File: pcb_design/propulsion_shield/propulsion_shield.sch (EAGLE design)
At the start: 62 parts

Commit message: [propulsion_shield] First draft of components placement + Bugfixes in schematics
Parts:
- JP14: value (none) -> M16PTH; device SparkFun-Connectors:M03PTH -> SparkFun-Connectors:M16PTH
- JP9: value M16PTH -> (none); device SparkFun-Connectors:M16PTH -> SparkFun-Connectors:M03PTH
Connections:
- net GND: now also JP14.1, JP9.2; no longer JP14.2, JP9.1
- net MOT1_1: now also JP5.2; no longer JP5.3
- net MOT1_2: now also JP5.3; no longer JP5.2
- net MOT2_1: now also JP6.2; no longer JP6.3
- net MOT2_2: now also JP6.3; no longer JP6.2
- net MOT3_1: now also JP7.2; no longer JP7.3
- net MOT3_2: now also JP7.3; no longer JP7.2
- net SCL_HW: no longer SJ2.2, SJ4.2
- net SDA_HW: now also SJ2.2, SJ4.2
- net SHARP_1: now also JP9.3; no longer JP10.3
- net SHARP_2: now also JP10.3; no longer JP11.3
- net SHARP_3: now also JP11.3; no longer JP12.3
- net SHARP_4: now also JP12.3; no longer JP13.3
- net SHARP_5: now also JP13.3; no longer JP14.3
- net UI_0: now also JP14.3; no longer JP9.3
- net UI_1: now also JP14.4; no longer JP9.4
- net UI_10: now also JP14.13; no longer JP9.13
- net UI_11: now also JP14.14; no longer JP9.14
- net UI_12: now also JP14.15; no longer JP9.15
- net UI_13: now also JP14.16; no longer JP9.16
- net UI_2: now also JP14.5; no longer JP9.5
- net UI_3: now also JP14.6; no longer JP9.6
- net UI_4: now also JP14.7; no longer JP9.7
- net UI_5: now also JP14.8; no longer JP9.8
- net UI_6: now also JP14.9; no longer JP9.9
- net UI_7: now also JP14.10; no longer JP9.10
- net UI_8: now also JP14.11; no longer JP9.11
- net UI_9: now also JP14.12; no longer JP9.12
- net VCC: now also JP14.2, JP9.1; no longer JP14.1, JP9.2
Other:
- moved on the sheet: JP10, JP11, JP12, JP13

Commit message: [propulsion_shield] Full routing of the PCB
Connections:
- net SCL_SW1: now also IC1.PK6(ADC14/PCINT22); no longer IC1.PK7(ADC15/PCINT23)
- net SDA_SW1: now also IC1.PK7(ADC15/PCINT23); no longer IC1.PK6(ADC14/PCINT22)
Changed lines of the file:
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@@
 <net name="SDA_SW1" class="0">
-<segment>
-<pinref part="IC1" gate="G$1" pin="PK6(ADC14/PCINT22)"/>
-<wire x1="15.24" y1="109.22" x2="2.54" y2="109.22" width="0.2032" layer="91"/>
-<label x="2.54" y="109.22" size="1.778" layer="95"/>
-</segment>
 <segment>
 <pinref part="JP22" gate="G$1" pin="1"/>
@@
 <label x="205.74" y="66.04" size="1.778" layer="95"/>
 </segment>
-</net>
-<net name="SCL_SW1" class="0">
 <segment>
 <pinref part="IC1" gate="G$1" pin="PK7(ADC15/PCINT23)"/>
@@
 <label x="2.54" y="106.68" size="1.778" layer="95"/>
 </segment>
+</net>
+<net name="SCL_SW1" class="0">
 <segment>
 <pinref part="JP22" gate="G$1" pin="2"/>
@@
 <label x="205.74" y="68.58" size="1.778" layer="95"/>
 </segment>
+<segment>
+<pinref part="IC1" gate="G$1" pin="PK6(ADC14/PCINT22)"/>
+<wire x1="15.24" y1="109.22" x2="2.54" y2="109.22" width="0.2032" layer="91"/>
+<label x="2.54" y="109.22" size="1.778" layer="95"/>
+</segment>
 </net>

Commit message: [propulsion_shield] Added Silkscreen on board
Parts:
- R13: value 470 -> 10k
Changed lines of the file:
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@@
 <part name="S2" library="SparkFun-Electromechanical" deviceset="SWITCH-MOMENTARY-2" device="PTH"/>
 <part name="GND33" library="SparkFun-Aesthetics" deviceset="GND" device=""/>
-<part name="R13" library="SparkFun-Passives" deviceset="RESISTOR" device="1206" value="470"/>
+<part name="R13" library="SparkFun-Passives" deviceset="RESISTOR" device="1206" value="10k"/>
 <part name="SUPPLY28" library="SparkFun-Aesthetics" deviceset="VCC" device=""/>
 <part name="JP28" library="SparkFun-Connectors" deviceset="M04" device="PTH"/>

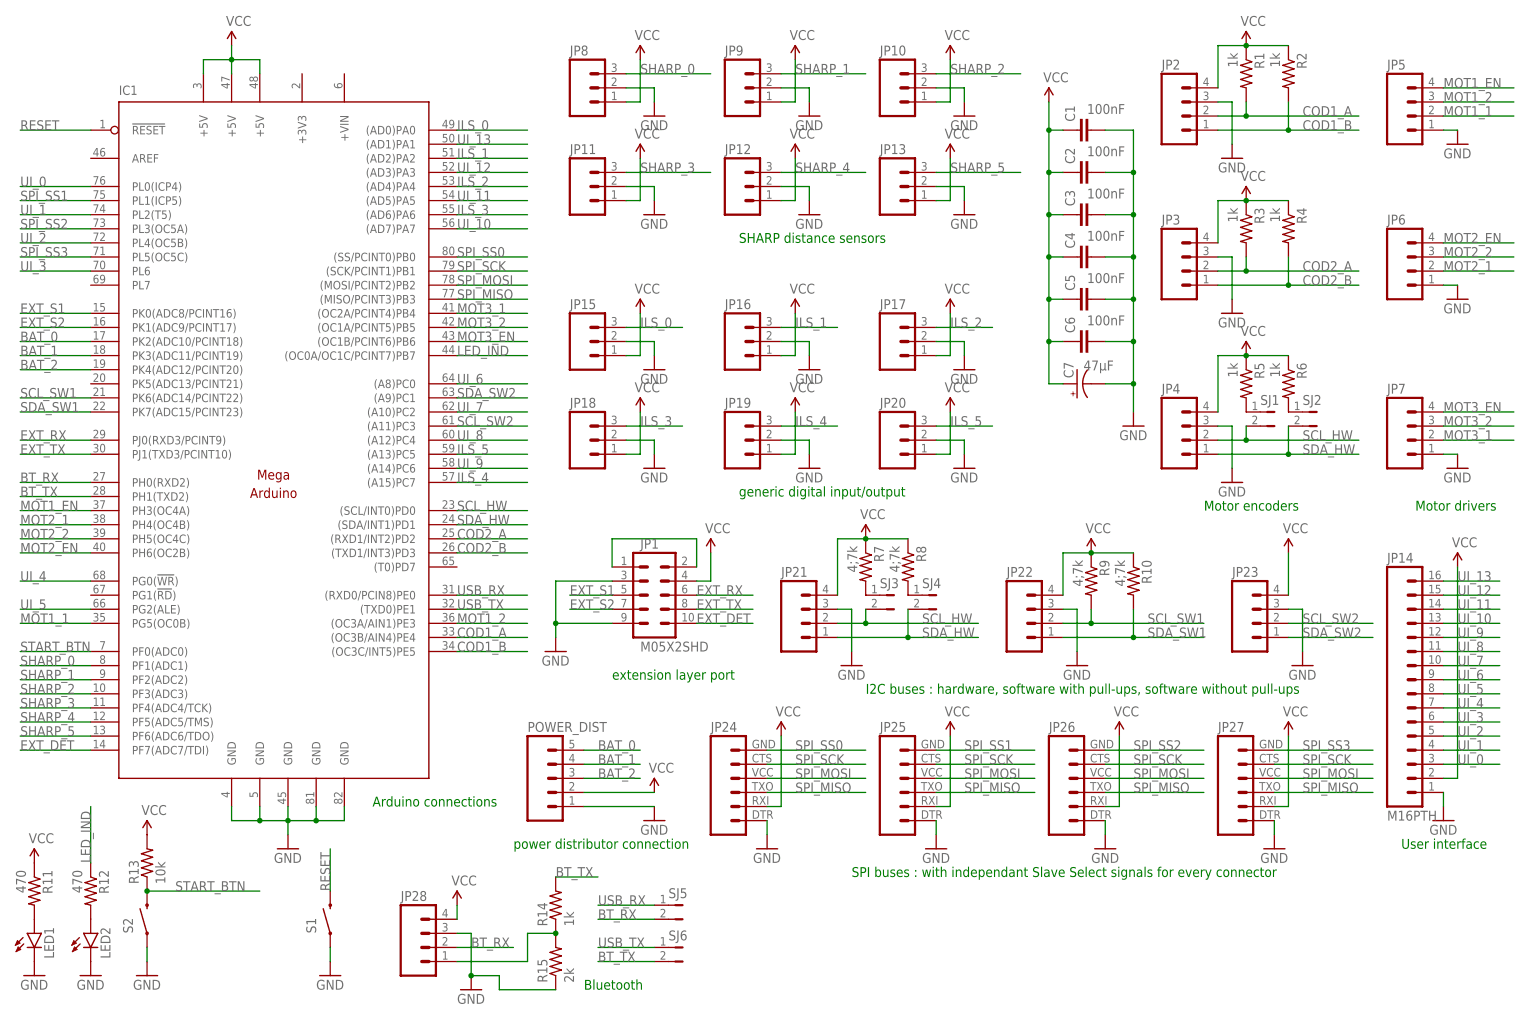
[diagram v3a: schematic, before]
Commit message: [propulsion_shield] Added a buzzer on the board
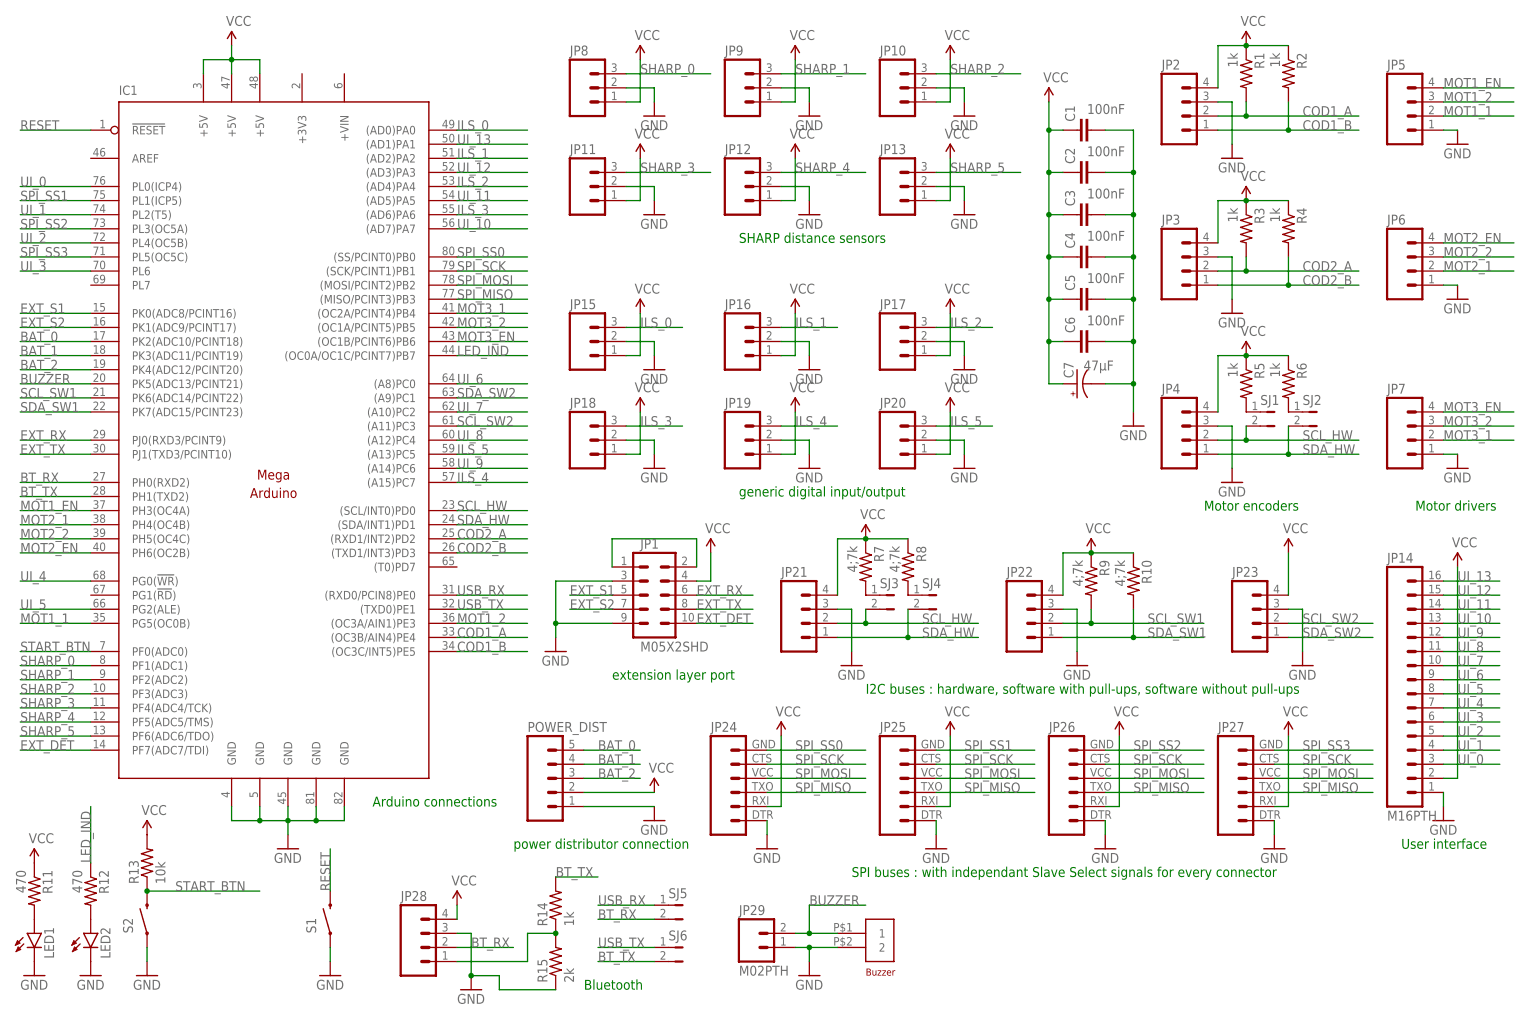
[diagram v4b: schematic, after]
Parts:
- added JP29: M02PTH, SparkFun-Connectors:M02PTH
- added U$1: BUZZER, buzzerG:BUZZER
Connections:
- new net BUZZER: IC1.PK5(ADC13/PCINT21), JP29.2, U$1.1
- net GND: now also JP29.1, U$1.2
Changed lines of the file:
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@@
 <part name="SUPPLY30" library="SparkFun-Aesthetics" deviceset="VCC" device=""/>
 <part name="GND35" library="SparkFun-Aesthetics" deviceset="GND" device=""/>
+<part name="U$1" library="buzzerG" deviceset="BUZZER" device=""/>
+<part name="JP29" library="SparkFun-Connectors" deviceset="M02" device="PTH"/>
+<part name="GND36" library="SparkFun-Aesthetics" deviceset="GND" device=""/>
 </parts>
 <sheets>
@@
 <instance part="SUPPLY30" gate="G$1" x="187.96" y="162.56"/>
 <instance part="GND35" gate="1" x="203.2" y="104.14"/>
+<instance part="U$1" gate="G$1" x="157.48" y="12.7"/>
+<instance part="JP29" gate="G$1" x="134.62" y="10.16"/>
+<instance part="GND36" gate="1" x="144.78" y="5.08"/>
 </instances>
 <busses>
@@
 <junction x="203.2" y="111.76"/>
 </segment>
+<segment>
+<pinref part="JP29" gate="G$1" pin="1"/>
+<pinref part="U$1" gate="G$1" pin="2"/>
+<wire x1="142.24" y1="10.16" x2="144.78" y2="10.16" width="0.1524" layer="91"/>
+<pinref part="GND36" gate="1" pin="GND"/>
+<wire x1="149.86" y1="10.16" x2="144.78" y2="10.16" width="0.1524" layer="91"/>
+<wire x1="144.78" y1="10.16" x2="144.78" y2="7.62" width="0.1524" layer="91"/>
+<junction x="144.78" y="10.16"/>
+</segment>
 </net>
 <net name="RESET" class="0">
@@
 </segment>
 </net>
+<net name="BUZZER" class="0">
+<segment>
+<pinref part="IC1" gate="G$1" pin="PK5(ADC13/PCINT21)"/>
+<wire x1="15.24" y1="111.76" x2="2.54" y2="111.76" width="0.1524" layer="91"/>
+<label x="2.54" y="111.76" size="1.778" layer="95"/>
+</segment>
+<segment>
+<pinref part="JP29" gate="G$1" pin="2"/>
+<pinref part="U$1" gate="G$1" pin="1"/>
+<wire x1="142.24" y1="12.7" x2="144.78" y2="12.7" width="0.1524" layer="91"/>
+<wire x1="149.86" y1="12.7" x2="144.78" y2="12.7" width="0.1524" layer="91"/>
+<wire x1="144.78" y1="12.7" x2="144.78" y2="17.78" width="0.1524" layer="91"/>
+<wire x1="144.78" y1="17.78" x2="154.94" y2="17.78" width="0.1524" layer="91"/>
+<label x="144.78" y="17.78" size="1.778" layer="95"/>
+<junction x="144.78" y="12.7"/>
+</segment>
+</net>
